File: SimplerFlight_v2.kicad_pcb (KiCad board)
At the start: 2 copper layers, 93.8 x 73.5 mm, 114 parts, among them J1 Battery 1, J10 Cam 3, J11 Servo, J12 Cam 2, J13 SWD Header, J14 DM3CS-SF, J2 Encoder, J7 Battery 2, J8 USB, J9 Cam 1, Q1 BSS816NWH6327XTSA1, Q2 NPN, Q3 BSS816NWH6327XTSA1, Q6 BSS816NWH6327XTSA1, SW1 Boot Switch, SW2 System Reset, U1 AMS1117-3.3, U2 STM32F401RETx, U3 BMP581, U4 BNO085, U5 TPS56A37RPAR, U6 TPS56A37RPAR, U7 MX25V4006EM1I-13G, Y2 Crystal

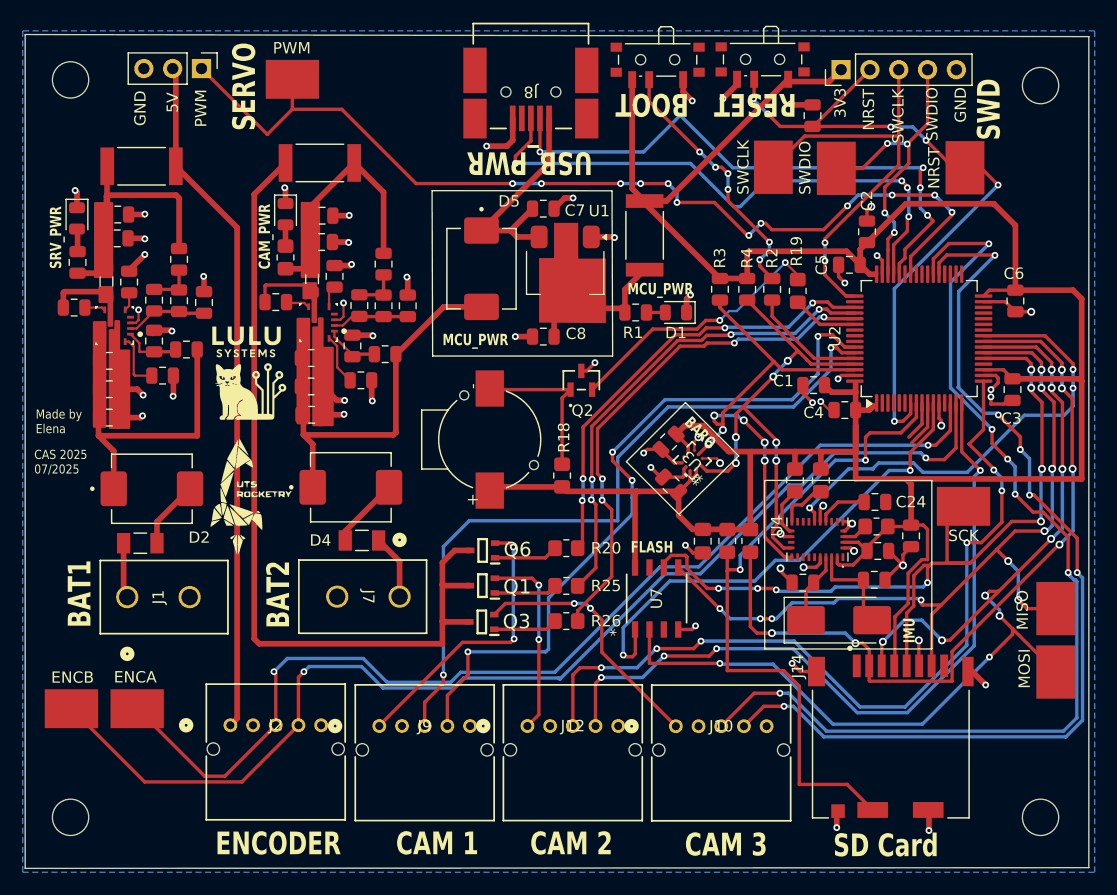
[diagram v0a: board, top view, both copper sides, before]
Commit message: remove camera power and interface headers and pins from schematic and PCB
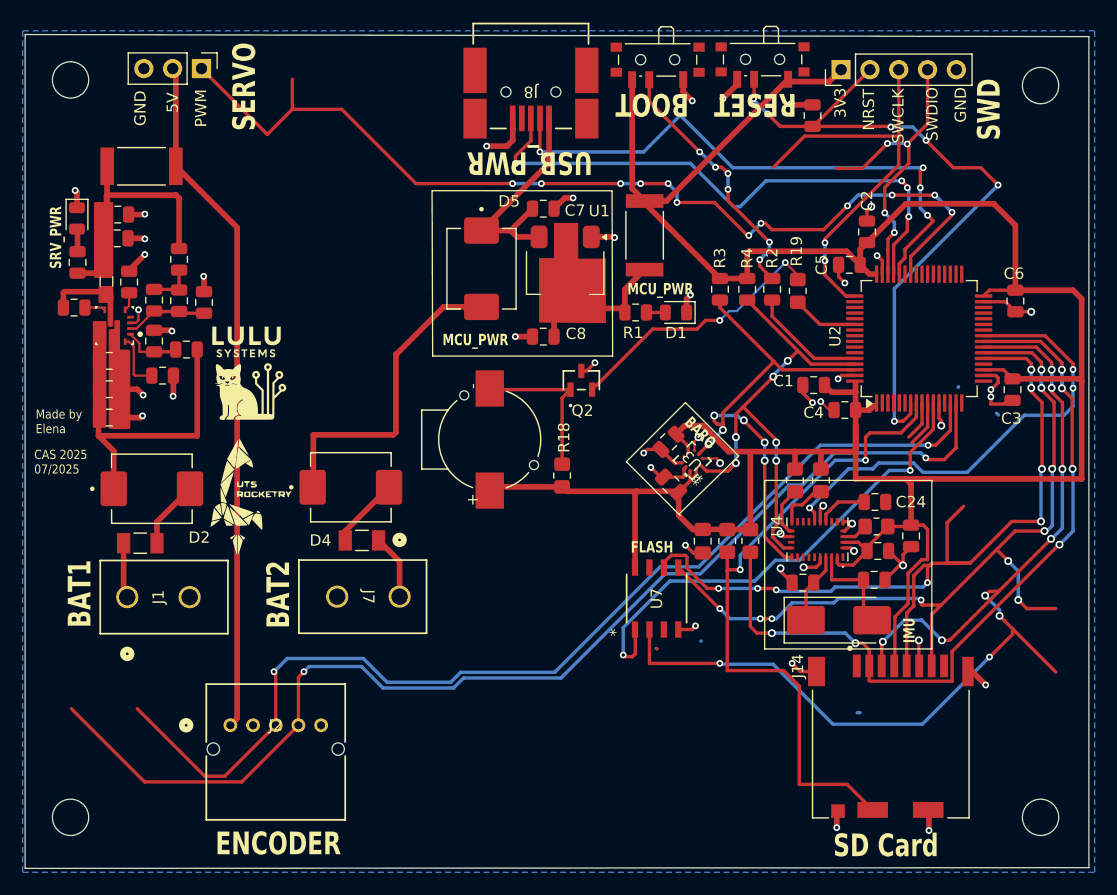
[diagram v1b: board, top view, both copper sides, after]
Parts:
- removed C18, C19, C38, C39: 10uF, Capacitor_SMD:C_0805_2012Metric
- removed C32, C36: 0.1uF, Capacitor_SMD:C_0805_2012Metric
- removed C33: 47nF, Capacitor_SMD:C_0805_2012Metric
- removed C37: 150pF, Capacitor_SMD:C_0805_2012Metric
- removed D7: RED, LED_SMD:LED_0805_2012Metric
- removed ENCA, ENCB, MISO, NRST, PWM, SCK, SWCLK, SWDIO: 5016, 5016:KEYSTONE_5016
- removed J10: Cam 3, S05B_PASK_2_LF__SN_:CONN_S05B-PASK-2_JST
- removed J12: Cam 2, S05B_PASK_2_LF__SN_:CONN_S05B-PASK-2_JST
- removed J9: Cam 1, S05B_PASK_2_LF__SN_:CONN_S05B-PASK-2_JST
- removed L2: 3.3uH, Inductor_SMD:L_0805_2012Metric_Pad1.05x1.20mm_HandSolder
- removed MOSI : 5016, 5016:KEYSTONE_5016
- removed Q1, Q3, Q6: BSS816NWH6327XTSA1, BSS816NWH6327XTSA1:SOT65P210X100-3N
- removed R12: 1k5, Resistor_SMD:R_0805_2012Metric_Pad1.20x1.40mm_HandSolder
- removed R20, R25, R26: 1kR, Resistor_SMD:R_0805_2012Metric_Pad1.20x1.40mm_HandSolder
- removed R21: 169kR, Capacitor_SMD:C_0805_2012Metric
- removed R22: 36.1kR, Capacitor_SMD:C_0805_2012Metric
- removed R23: 52.3kR, Capacitor_SMD:C_0805_2012Metric
- removed R24: 10kR, Capacitor_SMD:C_0805_2012Metric
- removed R27: CSRN2512FKR500, CSRN2512FKR500:RESC6331X70N
- removed R30: 49.9R, Capacitor_SMD:C_0805_2012Metric
- removed R31: 73.2kR, Capacitor_SMD:C_0805_2012Metric
- removed U6: TPS56A37RPAR, TPS56A37RPAR:RPA0010A-MFG
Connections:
- net /Power/VIN_CAM renamed Net-(D4-PadC)
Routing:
- net /Microcontroller/USART6_RX: track 89.6 -> 0.00 mm, vias 6 -> 0
- net /Microcontroller/USART6_TX: track 86.3 -> 0.29 mm, vias 6 -> 0
- net /Peripherals/5V_CAM: track 74.8 -> 0.00 mm
- net /Microcontroller/USART2_RX: track 72.2 -> 0.08 mm, vias 6 -> 0
- net /Microcontroller/USART2_TX: track 65.5 -> 0.25 mm, vias 4 -> 0
- net /Microcontroller/USART1_RX: track 64.6 -> 0.00 mm, vias 2 -> 0
- net /Microcontroller/USART1_TX: track 63.6 -> 0.00 mm, vias 4 -> 0
- net /Microcontroller/CAM_3_EN: track 45.6 -> 0.00 mm, vias 4 -> 0
- net /Microcontroller/CAM_2_EN: track 42.7 -> 0.00 mm, vias 4 -> 0
- net /Microcontroller/CAM_1_EN: track 39.6 -> 0.00 mm, vias 4 -> 0
- net /Peripherals/CAM_1_VO: track 25.0 -> 0.00 mm, vias 2 -> 0
- net /Peripherals/CAM_3_VO: track 22.6 -> 0.00 mm, vias 2 -> 0
- net /Power/5V_CAM: track 17.7 -> 0.00 mm
- net GND: track 117.9 -> 100.2 mm, vias 57 -> 47
- net /Peripherals/CAM_2_VO: track 17.0 -> 0.00 mm, vias 2 -> 0
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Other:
- board text removed: "CAM 1"
- board text removed: "CAM 2"
- board text removed: "CAM 3"
- board text removed: "CAM_PWR"
